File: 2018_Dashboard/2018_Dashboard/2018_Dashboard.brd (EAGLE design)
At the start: 127 x 58.4 mm, 53 parts, among them Y1 16MHz

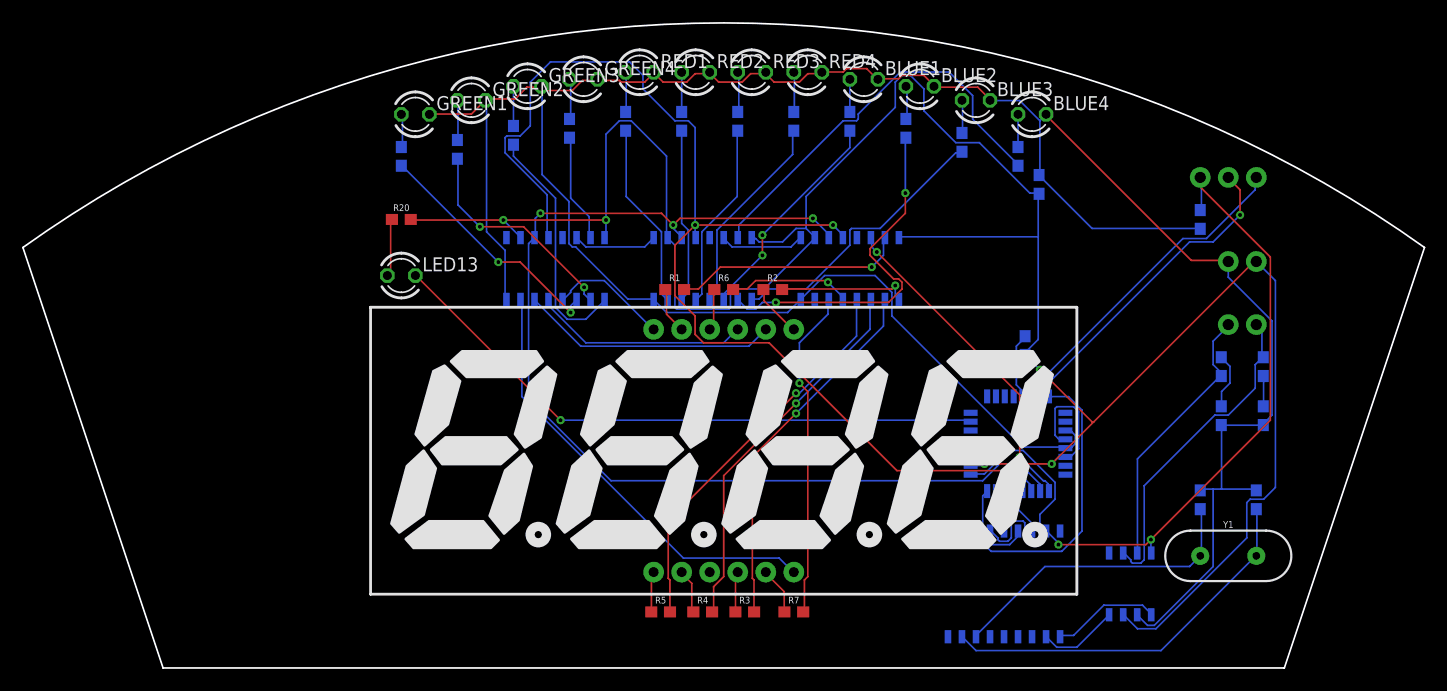
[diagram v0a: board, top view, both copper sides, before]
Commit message: Changed resistors from before seven segment to after seven segment, reduced number of resistors
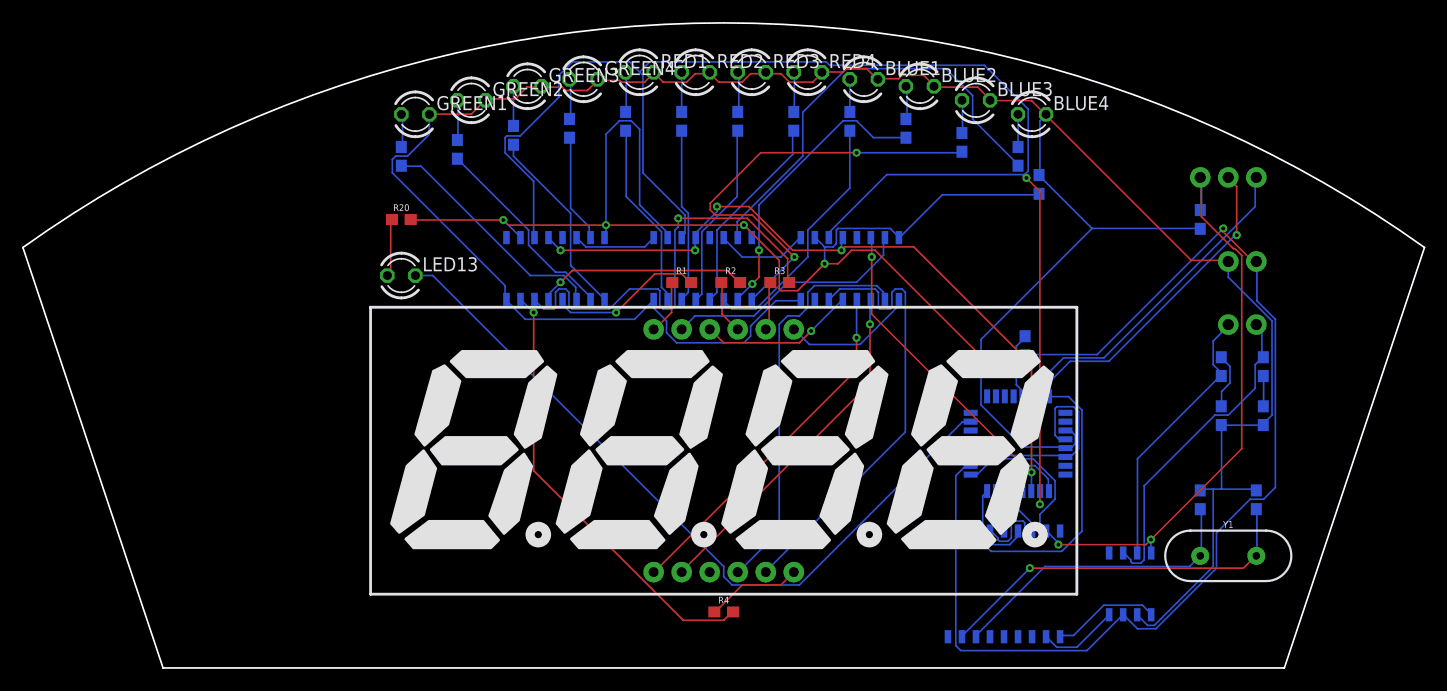
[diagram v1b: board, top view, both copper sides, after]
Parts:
- removed R5, R6, R7: 330, SparkFun-Resistors:0603
- moved R3 30.0 mm to (47.0, 52.7)
- moved R2 3.86 mm to (42.5, 52.7)
- moved R4 1.90 mm to (41.9, 22.9)
- moved R1 0.90 mm to (38.1, 52.7)
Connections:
- removed net N$7: R5.2, SHIFT_1.4
- removed net N$8: R6.2, SHIFT_1.5
- removed net N$9: R7.2, SHIFT_1.6
- net N$11: now also SHIFT_1.15; no longer R1.1
- net N$12: now also SHIFT_1.1; no longer R2.1
- net N$13: now also SHIFT_1.2; no longer R3.1
- net N$14: now also SHIFT_1.3; no longer R4.1
- net N$15: now also SHIFT_1.4; no longer R5.1
- net N$16: now also SHIFT_1.5; no longer R6.1
- net N$17: now also SHIFT_1.6; no longer R7.1
- net N$24: now also R1.1; no longer SHIFT_3.4
- net N$3: now also SHIFT_3.4; no longer SHIFT_1.15
- net N$4: now also SHIFT_3.5; no longer SHIFT_1.1
- net N$47: now also R2.1; no longer SHIFT_3.5
- net N$48: now also R3.1; no longer SHIFT_3.6
- net N$49: now also R4.1; no longer SHIFT_3.7
- net N$5: now also SHIFT_3.6; no longer SHIFT_1.2
- net N$6: now also SHIFT_3.7; no longer SHIFT_1.3
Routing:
- net N$22: track 108.4 -> 65.9 mm, vias 3 -> 5
- net N$21: track 97.8 -> 139.1 mm, vias 3 -> 2
- net N$17: track 4.31 -> 41.2 mm
- net N$7: track 35.6 -> 0.00 mm, vias 1 -> 0
- net N$13: track 3.69 -> 36.7 mm
- net N$49: track 40.1 -> 8.69 mm
- net N$9: track 30.0 -> 0.00 mm, vias 1 -> 0
- net N$15: track 3.69 -> 32.3 mm, vias 0 -> 1
- net N$14: track 4.13 -> 31.8 mm, vias 0 -> 1
- net N$48: track 23.4 -> 4.41 mm
- net N$11: track 4.23 -> 22.7 mm
- net N$26: track 25.4 -> 40.2 mm, vias 0 -> 2
- net N$47: track 19.6 -> 4.88 mm
- net N$51: track 55.8 -> 68.6 mm, vias 1 -> 0
- net N$8: track 11.2 -> 0.00 mm, vias 1 -> 0
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
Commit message: Added silkscreen stuff
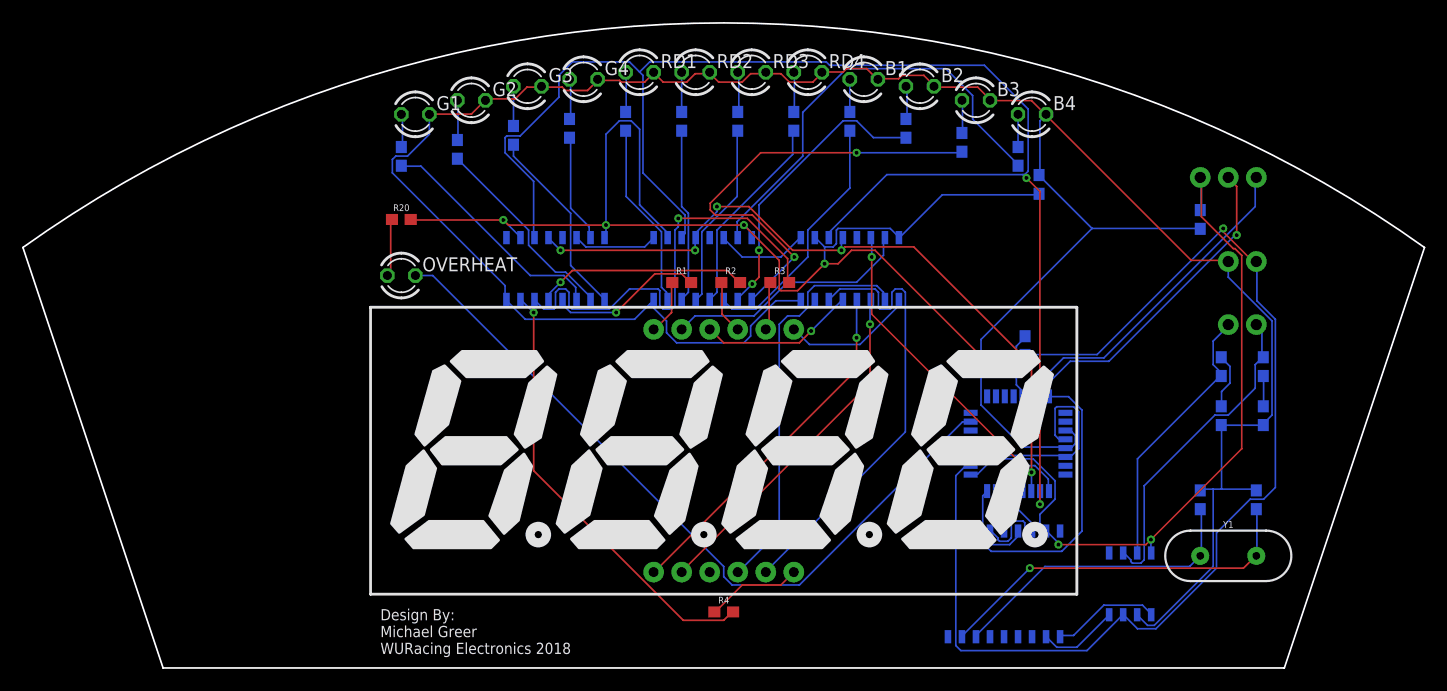
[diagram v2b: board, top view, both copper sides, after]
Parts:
- B1, B2, B3, B4, G1, G2, G3, G4, OVERHEAT, RD1, RD2, RD3, RD4: value TLLG4400 -> (none)
- renumbered BLUE1 to B1, BLUE2 to B2, BLUE3 to B3, BLUE4 to B4, GREEN1 to G1, GREEN2 to G2, GREEN3 to G3, GREEN4 to G4, LED13 to OVERHEAT, RED1 to RD1, RED2 to RD2, RED3 to RD3, RED4 to RD4
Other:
- board text added: "Design By: Michael Greer WURacing Electronics 2018"
